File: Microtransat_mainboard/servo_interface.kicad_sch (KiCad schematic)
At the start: 3 parts, among them J11 Conn_01x03, J12 Conn_01x03, J13 Conn_01x03

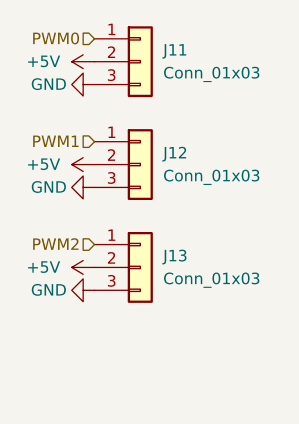
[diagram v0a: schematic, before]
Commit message: Added new IMU to the schematic + new PWM
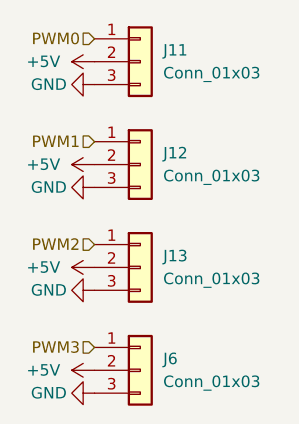
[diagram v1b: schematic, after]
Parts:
- added J6: Conn_01x03, symbol Connector_Generic:Conn_01x03
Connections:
- net +5V: now also J6.2 (Pin_2)
- net GND: now also J6.3 (Pin_3)
- new net PWM3: J6.1 (Pin_1)
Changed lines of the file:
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@@
 	(generator_version "9.0")
 	(paper "A4")
+	(hierarchical_label "PWM3"
+		(shape input)
+		(at 83.82 102.87 180)
+		(effects
+			(font
+				(size 1.27 1.27)
+			)
+			(justify right)
+		)
+	)
 	(hierarchical_label "PWM2"
 		(shape input)
@@
 	(symbol
 		(lib_id "Connector_Generic:Conn_01x03")
+		(at 88.9 105.41 0)
+		(unit 1)
+		(exclude_from_sim no)
+		(in_bom yes)
+		(on_board yes)
+		(dnp no)
+		(fields_autoplaced yes)
+		(property "Reference" "J6"
+			(at 91.44 104.1399 0)
+			(effects
+				(font
+					(size 1.27 1.27)
+				)
+				(justify left)
+			)
+		)
+		(property "Value" "Conn_01x03"
+			(at 91.44 106.6799 0)
+			(effects
+				(font
+					(size 1.27 1.27)
+				)
+				(justify left)
+			)
+		)
+		(property "Footprint" ""
+			(at 88.9 105.41 0)
+			(effects
+				(font
+					(size 1.27 1.27)
+				)
+				(hide yes)
+			)
+		)
+		(property "Datasheet" "~"
+			(at 88.9 105.41 0)
+			(effects
+				(font
+					(size 1.27 1.27)
+				)
+				(hide yes)
+			)
+		)
+		(property "Description" "Generic connector, single row, 01x03, script generated (kicad-library-utils/schlib/autogen/connector/)"
+			(at 88.9 105.41 0)
+			(effects
+				(font
+					(size 1.27 1.27)
+				)
+				(hide yes)
+			)
+		)
+		(pin "3"
+		)
+		(pin "2"
+		)
+		(pin "1"
+		)
+		(instances
+			(project "Microtransat_mainboard"
+				(path "/89914625-be83-416e-bb0d-b792f59b4aa6/a04f4943-a262-4b21-933a-c8835e5cae79"
+					(reference "J6")
+					(unit 1)
+				)
+			)
+		)
+	)
+	(symbol
+		(lib_id "Connector_Generic:Conn_01x03")
 		(at 88.9 93.98 0)
 		(unit 1)
@@
 	)
 	(symbol
+		(lib_id "power:+5V")
+		(at 83.82 105.41 90)
+		(unit 1)
+		(exclude_from_sim no)
+		(in_bom yes)
+		(on_board yes)
+		(dnp no)
+		(fields_autoplaced yes)
+		(property "Reference" "#PWR010"
+			(at 87.63 105.41 0)
+			(effects
+				(font
+					(size 1.27 1.27)
+				)
+				(hide yes)
+			)
+		)
+		(property "Value" "+5V"
+			(at 80.01 105.4099 90)
+			(effects
+				(font
+					(size 1.27 1.27)
+				)
+				(justify left)
+			)
+		)
+		(property "Footprint" ""
+			(at 83.82 105.41 0)
+			(effects
+				(font
+					(size 1.27 1.27)
+				)
+				(hide yes)
+			)
+		)
+		(property "Datasheet" ""
+			(at 83.82 105.41 0)
+			(effects
+				(font
+					(size 1.27 1.27)
+				)
+				(hide yes)
+			)
+		)
+		(property "Description" "Power symbol creates a global label with name \"+5V\""
+			(at 83.82 105.41 0)
+			(effects
+				(font
+					(size 1.27 1.27)
+				)
+				(hide yes)
+			)
+		)
+		(pin "1"
+		)
+		(instances
+			(project "Microtransat_mainboard"
+				(path "/89914625-be83-416e-bb0d-b792f59b4aa6/a04f4943-a262-4b21-933a-c8835e5cae79"
+					(reference "#PWR010")
+					(unit 1)
+				)
+			)
+		)
+	)
+	(symbol
 		(lib_id "Connector_Generic:Conn_01x03")
 		(at 88.9 71.12 0)
@@
 					(unit 1)
 				)
+			)
+		)
+	)
+	(symbol
+		(lib_id "power:GND")
+		(at 83.82 107.95 270)
+		(unit 1)
+		(exclude_from_sim no)
+		(in_bom yes)
+		(on_board yes)
+		(dnp no)
+		(property "Reference" "#PWR09"
+			(at 77.47 107.95 0)
+			(effects
+				(font
+					(size 1.27 1.27)
+				)
+				(hide yes)
+			)
+		)
+		(property "Value" "GND"
+			(at 78.74 107.95 90)
+			(effects
+				(font
+					(size 1.27 1.27)
+				)
+			)
+		)
+		(property "Footprint" ""
+			(at 83.82 107.95 0)
+			(effects
+				(font
+					(size 1.27 1.27)
+				)
+				(hide yes)
+			)
+		)
+		(property "Datasheet" ""
+			(at 83.82 107.95 0)
+			(effects
+				(font
+					(size 1.27 1.27)
+				)
+				(hide yes)
+			)
+		)
+		(property "Description" "Power symbol creates a global label with name \"GND\" , ground"
+			(at 83.82 107.95 0)
+			(effects
+				(font
+					(size 1.27 1.27)
+				)
+				(hide yes)
+			)
+		)
+		(pin "1"
+		)
+		(instances
+			(project "Microtransat_mainboard"
+				(path "/89914625-be83-416e-bb0d-b792f59b4aa6/a04f4943-a262-4b21-933a-c8835e5cae79"
+					(reference "#PWR09")
+					(unit 1)
+				)

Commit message: Fixed ERC errors
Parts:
- J11, J12, J13, J6: footprint (none) -> Connector_JST:JST_XH_S3B-XH-A_1x03_P2.50mm_Horizontal
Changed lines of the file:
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@@
 			)
 		)
-		(property "Footprint" ""
+		(property "Footprint" "Connector_JST:JST_XH_S3B-XH-A_1x03_P2.50mm_Horizontal"
 			(at 88.9 105.41 0)
 			(effects
@@
 			)
 		)
-		(property "Footprint" ""
+		(property "Footprint" "Connector_JST:JST_XH_S3B-XH-A_1x03_P2.50mm_Horizontal"
 			(at 88.9 93.98 0)
 			(effects
@@
 			)
 		)
-		(property "Footprint" ""
+		(property "Footprint" "Connector_JST:JST_XH_S3B-XH-A_1x03_P2.50mm_Horizontal"
 			(at 88.9 71.12 0)
 			(effects
@@
 			)
 		)
-		(property "Footprint" ""
+		(property "Footprint" "Connector_JST:JST_XH_S3B-XH-A_1x03_P2.50mm_Horizontal"
 			(at 88.9 82.55 0)
 			(effects

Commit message: Updated footprints
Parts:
- J11, J12, J13, J6: footprint Connector_JST:JST_XH_S3B-XH-A_1x03_P2.50mm_Horizontal -> Connector_JST:JST_XH_B3B-XH-A_1x03_P2.50mm_Vertical
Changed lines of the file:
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@@
 			)
 		)
-		(property "Footprint" "Connector_JST:JST_XH_S3B-XH-A_1x03_P2.50mm_Horizontal"
+		(property "Footprint" "Connector_JST:JST_XH_B3B-XH-A_1x03_P2.50mm_Vertical"
 			(at 88.9 105.41 0)
 			(effects
@@
 			)
 		)
-		(property "Footprint" "Connector_JST:JST_XH_S3B-XH-A_1x03_P2.50mm_Horizontal"
+		(property "Footprint" "Connector_JST:JST_XH_B3B-XH-A_1x03_P2.50mm_Vertical"
 			(at 88.9 93.98 0)
 			(effects
@@
 			)
 		)
-		(property "Footprint" "Connector_JST:JST_XH_S3B-XH-A_1x03_P2.50mm_Horizontal"
+		(property "Footprint" "Connector_JST:JST_XH_B3B-XH-A_1x03_P2.50mm_Vertical"
 			(at 88.9 71.12 0)
 			(effects
@@
 			)
 		)
-		(property "Footprint" "Connector_JST:JST_XH_S3B-XH-A_1x03_P2.50mm_Horizontal"
+		(property "Footprint" "Connector_JST:JST_XH_B3B-XH-A_1x03_P2.50mm_Vertical"
 			(at 88.9 82.55 0)
 			(effects

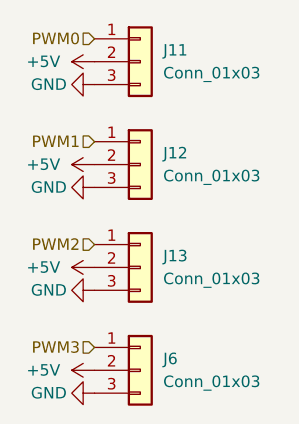
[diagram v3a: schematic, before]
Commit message: Finished silkscreen/outline changes
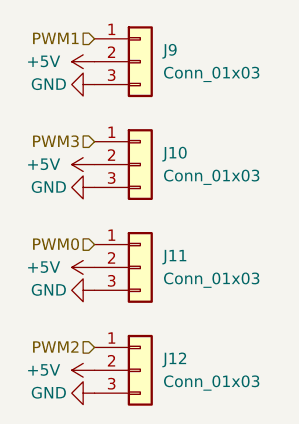
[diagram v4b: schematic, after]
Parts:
- renumbered J12 to J10, J13 to J11, J6 to J12, J11 to J9
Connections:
- net PWM0: now also J11.1 (Pin_1); no longer J9.1 (Pin_1)
- net PWM1: now also J9.1 (Pin_1); no longer J10.1 (Pin_1)
- net PWM2: now also J12.1 (Pin_1); no longer J11.1 (Pin_1)
- net PWM3: now also J10.1 (Pin_1); no longer J12.1 (Pin_1)
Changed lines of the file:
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@@
 	(generator_version "9.0")
 	(paper "A4")
-	(hierarchical_label "PWM3"
+	(hierarchical_label "PWM2"
 		(shape input)
 		(at 83.82 102.87 180)
@@
 		)
 	)
-	(hierarchical_label "PWM2"
+	(hierarchical_label "PWM0"
 		(shape input)
 		(at 83.82 91.44 180)
@@
 		)
 	)
-	(hierarchical_label "PWM0"
+	(hierarchical_label "PWM1"
 		(shape input)
 		(at 83.82 68.58 180)
@@
 		)
 	)
-	(hierarchical_label "PWM1"
+	(hierarchical_label "PWM3"
 		(shape input)
 		(at 83.82 80.01 180)
@@
 		(dnp no)
 		(fields_autoplaced yes)
-		(property "Reference" "J6"
+		(property "Reference" "J12"
 			(at 91.44 104.1399 0)
 			(effects
@@
 			(project "Microtransat_mainboard"
 				(path "/89914625-be83-416e-bb0d-b792f59b4aa6/a04f4943-a262-4b21-933a-c8835e5cae79"
-					(reference "J6")
+					(reference "J12")
 					(unit 1)
 				)
@@
 		(dnp no)
 		(fields_autoplaced yes)
-		(property "Reference" "J13"
+		(property "Reference" "J11"
 			(at 91.44 92.7099 0)
 			(effects
@@
 			(project "Microtransat_mainboard"
 				(path "/89914625-be83-416e-bb0d-b792f59b4aa6/a04f4943-a262-4b21-933a-c8835e5cae79"
-					(reference "J13")
+					(reference "J11")
 					(unit 1)
 				)
@@
 		(on_board yes)
 		(dnp no)
-		(property "Reference" "#PWR06"
+		(property "Reference" "#PWR038"
 			(at 77.47 85.09 0)
 			(effects
@@
 			(project "Microtransat_mainboard"
 				(path "/89914625-be83-416e-bb0d-b792f59b4aa6/a04f4943-a262-4b21-933a-c8835e5cae79"
-					(reference "#PWR06")
+					(reference "#PWR038")
 					(unit 1)
 				)
@@
 		(dnp no)
 		(fields_autoplaced yes)
-		(property "Reference" "#PWR010"
+		(property "Reference" "#PWR041"
 			(at 87.63 105.41 0)
 			(effects
@@
 			(project "Microtransat_mainboard"
 				(path "/89914625-be83-416e-bb0d-b792f59b4aa6/a04f4943-a262-4b21-933a-c8835e5cae79"
-					(reference "#PWR010")
+					(reference "#PWR041")
 					(unit 1)
 				)
@@
 		(dnp no)
 		(fields_autoplaced yes)
-		(property "Reference" "J11"
+		(property "Reference" "J9"
 			(at 91.44 69.8499 0)
 			(effects
@@
 			(project "Microtransat_mainboard"
 				(path "/89914625-be83-416e-bb0d-b792f59b4aa6/a04f4943-a262-4b21-933a-c8835e5cae79"
-					(reference "J11")
+					(reference "J9")
 					(unit 1)
 				)
@@
 		(dnp no)
 		(fields_autoplaced yes)
-		(property "Reference" "#PWR03"
+		(property "Reference" "#PWR035"
 			(at 87.63 71.12 0)
 			(effects
@@
 			(project "Microtransat_mainboard"
 				(path "/89914625-be83-416e-bb0d-b792f59b4aa6/a04f4943-a262-4b21-933a-c8835e5cae79"
-					(reference "#PWR03")
+					(reference "#PWR035")
 					(unit 1)
 				)
@@
 		(on_board yes)
 		(dnp no)
-		(property "Reference" "#PWR016"
+		(property "Reference" "#PWR040"
 			(at 77.47 96.52 0)
 			(effects
@@
 			(project "Microtransat_mainboard"
 				(path "/89914625-be83-416e-bb0d-b792f59b4aa6/a04f4943-a262-4b21-933a-c8835e5cae79"
-					(reference "#PWR016")
+					(reference "#PWR040")
 					(unit 1)
 				)
@@
 		(dnp no)
 		(fields_autoplaced yes)
-		(property "Reference" "J12"
+		(property "Reference" "J10"
 			(at 91.44 81.2799 0)
 			(effects
@@
 			(project "Microtransat_mainboard"
 				(path "/89914625-be83-416e-bb0d-b792f59b4aa6/a04f4943-a262-4b21-933a-c8835e5cae79"
-					(reference "J12")
+					(reference "J10")
 					(unit 1)
 				)
@@
 		(on_board yes)
 		(dnp no)
-		(property "Reference" "#PWR04"
+		(property "Reference" "#PWR036"
 			(at 77.47 73.66 0)
 			(effects
@@
 			(project "Microtransat_mainboard"
 				(path "/89914625-be83-416e-bb0d-b792f59b4aa6/a04f4943-a262-4b21-933a-c8835e5cae79"
-					(reference "#PWR04")
+					(reference "#PWR036")
 					(unit 1)
 				)
@@
 		(on_board yes)
 		(dnp no)
-		(property "Reference" "#PWR09"
+		(property "Reference" "#PWR042"
 			(at 77.47 107.95 0)
 			(effects
@@
 			(project "Microtransat_mainboard"
 				(path "/89914625-be83-416e-bb0d-b792f59b4aa6/a04f4943-a262-4b21-933a-c8835e5cae79"
-					(reference "#PWR09")
+					(reference "#PWR042")
 					(unit 1)
 				)
@@
 		(dnp no)
 		(fields_autoplaced yes)
-		(property "Reference" "#PWR05"
+		(property "Reference" "#PWR037"
 			(at 87.63 82.55 0)
 			(effects
@@
 			(project "Microtransat_mainboard"
 				(path "/89914625-be83-416e-bb0d-b792f59b4aa6/a04f4943-a262-4b21-933a-c8835e5cae79"
-					(reference "#PWR05")
+					(reference "#PWR037")
 					(unit 1)
 				)
@@
 		(dnp no)
 		(fields_autoplaced yes)
-		(property "Reference" "#PWR015"
+		(property "Reference" "#PWR039"
 			(at 87.63 93.98 0)
 			(effects
@@
 			(project "Microtransat_mainboard"
 				(path "/89914625-be83-416e-bb0d-b792f59b4aa6/a04f4943-a262-4b21-933a-c8835e5cae79"
-					(reference "#PWR015")
-					(unit 1)
-				)
+					(reference "#PWR039")
+					(unit 1)
+				)

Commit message: Some small changes to silkscreen and component numbers
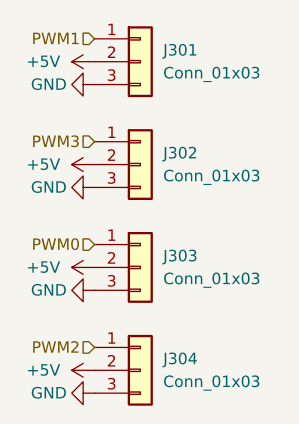
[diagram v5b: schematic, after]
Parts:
- renumbered J9 to J301, J10 to J302, J11 to J303, J12 to J304
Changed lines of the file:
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@@
 		(dnp no)
 		(fields_autoplaced yes)
-		(property "Reference" "J12"
+		(property "Reference" "J304"
 			(at 91.44 104.1399 0)
 			(effects
@@
 			(project "Microtransat_mainboard"
 				(path "/89914625-be83-416e-bb0d-b792f59b4aa6/a04f4943-a262-4b21-933a-c8835e5cae79"
-					(reference "J12")
+					(reference "J304")
 					(unit 1)
 				)
@@
 		(dnp no)
 		(fields_autoplaced yes)
-		(property "Reference" "J11"
+		(property "Reference" "J303"
 			(at 91.44 92.7099 0)
 			(effects
@@
 			(project "Microtransat_mainboard"
 				(path "/89914625-be83-416e-bb0d-b792f59b4aa6/a04f4943-a262-4b21-933a-c8835e5cae79"
-					(reference "J11")
+					(reference "J303")
 					(unit 1)
 				)
@@
 		(on_board yes)
 		(dnp no)
-		(property "Reference" "#PWR038"
+		(property "Reference" "#PWR0304"
 			(at 77.47 85.09 0)
 			(effects
@@
 			(project "Microtransat_mainboard"
 				(path "/89914625-be83-416e-bb0d-b792f59b4aa6/a04f4943-a262-4b21-933a-c8835e5cae79"
-					(reference "#PWR038")
+					(reference "#PWR0304")
 					(unit 1)
 				)
@@
 		(dnp no)
 		(fields_autoplaced yes)
-		(property "Reference" "#PWR041"
+		(property "Reference" "#PWR0307"
 			(at 87.63 105.41 0)
 			(effects
@@
 			(project "Microtransat_mainboard"
 				(path "/89914625-be83-416e-bb0d-b792f59b4aa6/a04f4943-a262-4b21-933a-c8835e5cae79"
-					(reference "#PWR041")
+					(reference "#PWR0307")
 					(unit 1)
 				)
@@
 		(dnp no)
 		(fields_autoplaced yes)
-		(property "Reference" "J9"
+		(property "Reference" "J301"
 			(at 91.44 69.8499 0)
 			(effects
@@
 			(project "Microtransat_mainboard"
 				(path "/89914625-be83-416e-bb0d-b792f59b4aa6/a04f4943-a262-4b21-933a-c8835e5cae79"
-					(reference "J9")
+					(reference "J301")
 					(unit 1)
 				)
@@
 		(dnp no)
 		(fields_autoplaced yes)
-		(property "Reference" "#PWR035"
+		(property "Reference" "#PWR0301"
 			(at 87.63 71.12 0)
 			(effects
@@
 			(project "Microtransat_mainboard"
 				(path "/89914625-be83-416e-bb0d-b792f59b4aa6/a04f4943-a262-4b21-933a-c8835e5cae79"
-					(reference "#PWR035")
+					(reference "#PWR0301")
 					(unit 1)
 				)
@@
 		(on_board yes)
 		(dnp no)
-		(property "Reference" "#PWR040"
+		(property "Reference" "#PWR0306"
 			(at 77.47 96.52 0)
 			(effects
@@
 			(project "Microtransat_mainboard"
 				(path "/89914625-be83-416e-bb0d-b792f59b4aa6/a04f4943-a262-4b21-933a-c8835e5cae79"
-					(reference "#PWR040")
+					(reference "#PWR0306")
 					(unit 1)
 				)
@@
 		(dnp no)
 		(fields_autoplaced yes)
-		(property "Reference" "J10"
+		(property "Reference" "J302"
 			(at 91.44 81.2799 0)
 			(effects
@@
 			(project "Microtransat_mainboard"
 				(path "/89914625-be83-416e-bb0d-b792f59b4aa6/a04f4943-a262-4b21-933a-c8835e5cae79"
-					(reference "J10")
+					(reference "J302")
 					(unit 1)
 				)
@@
 		(on_board yes)
 		(dnp no)
-		(property "Reference" "#PWR036"
+		(property "Reference" "#PWR0302"
 			(at 77.47 73.66 0)
 			(effects
@@
 			(project "Microtransat_mainboard"
 				(path "/89914625-be83-416e-bb0d-b792f59b4aa6/a04f4943-a262-4b21-933a-c8835e5cae79"
-					(reference "#PWR036")
+					(reference "#PWR0302")
 					(unit 1)
 				)
@@
 		(on_board yes)
 		(dnp no)
-		(property "Reference" "#PWR042"
+		(property "Reference" "#PWR0308"
 			(at 77.47 107.95 0)
 			(effects
@@
 			(project "Microtransat_mainboard"
 				(path "/89914625-be83-416e-bb0d-b792f59b4aa6/a04f4943-a262-4b21-933a-c8835e5cae79"
-					(reference "#PWR042")
+					(reference "#PWR0308")
 					(unit 1)
 				)
@@
 		(dnp no)
 		(fields_autoplaced yes)
-		(property "Reference" "#PWR037"
+		(property "Reference" "#PWR0303"
 			(at 87.63 82.55 0)
 			(effects
@@
 			(project "Microtransat_mainboard"
 				(path "/89914625-be83-416e-bb0d-b792f59b4aa6/a04f4943-a262-4b21-933a-c8835e5cae79"
-					(reference "#PWR037")
+					(reference "#PWR0303")
 					(unit 1)
 				)
@@
 		(dnp no)
 		(fields_autoplaced yes)
-		(property "Reference" "#PWR039"
+		(property "Reference" "#PWR0305"
 			(at 87.63 93.98 0)
 			(effects
@@
 			(project "Microtransat_mainboard"
 				(path "/89914625-be83-416e-bb0d-b792f59b4aa6/a04f4943-a262-4b21-933a-c8835e5cae79"
-					(reference "#PWR039")
-					(unit 1)
-				)
+					(reference "#PWR0305")
+					(unit 1)
+				)
